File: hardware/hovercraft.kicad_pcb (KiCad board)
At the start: 2 copper layers, 50 x 65 mm, 44 parts, among them J1 USB_OTG, J10 CONN_01X02, J11 CONN_01X02, J12 CONN_01X02, J2 CONN_01X03, J3 CONN_01X03, J4 CONN_01X03, J5 CONN_01X03, J6 CONN_01X03, J7 CONN_01X03, J8 CONN_01X02, J9 CONN_01X02, SW1 RESET, SW2 BOOT, U1 HC-12, U2 ATMEGA32U2-AU, Y1 Crystal_GND24

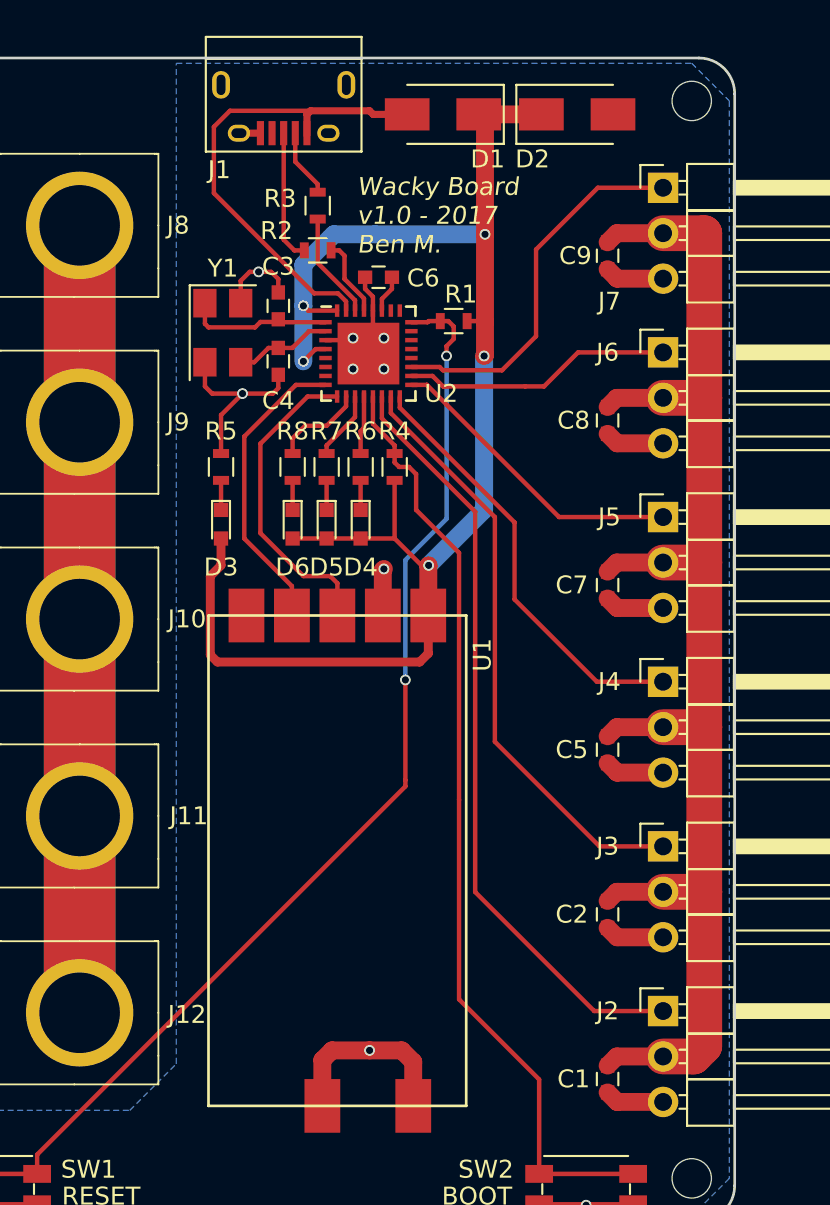
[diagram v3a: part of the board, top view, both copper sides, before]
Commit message: Moved the servo PWM signals to different pins to free up the SPI for a gyroscope/accelerometer/magnetometer
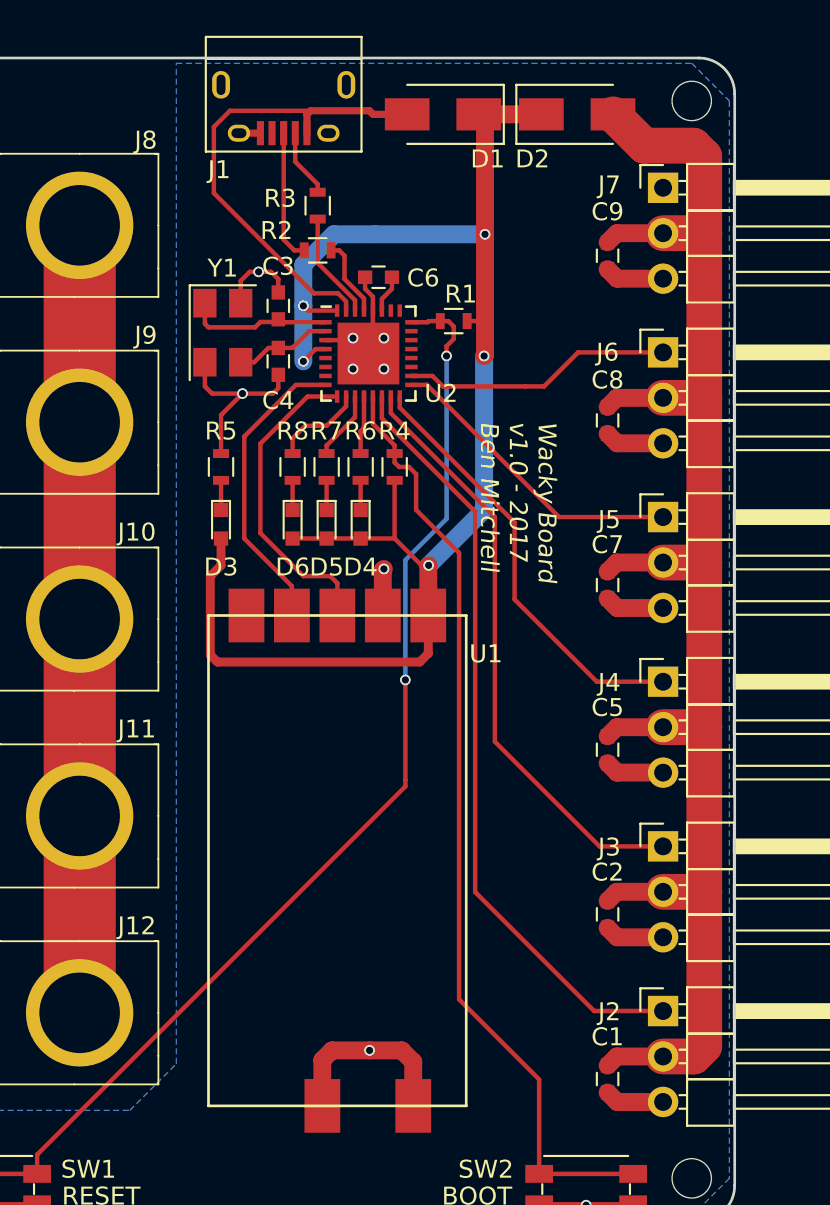
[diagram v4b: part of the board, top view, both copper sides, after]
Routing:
- net /CH5: track 21.2 -> 0.00 mm
- net Net-(C1-Pad1): track 79.3 -> 89.7 mm
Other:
- board text added: "Wacky Board v1.0 - 2017 Ben Mitchell"
- board text removed: "Wacky Board v1.0 - 2017 Ben M."
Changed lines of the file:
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@@
     (area 99.984999 100.004999 150.135001 165.155001)
     (thickness 1.6)
-    (drawings 11)
-    (tracks 288)
+    (drawings 13)
+    (tracks 285)
     (zones 0)
     (modules 44)
@@
   )
   (setup
-    (last_trace_width 0.25)
+    (last_trace_width 2)
     (user_trace_width 0.4)
     (user_trace_width 0.5)
@@
     (tags "capacitor 0603")
     (attr smd)
-    (fp_text reference C2 (at 0 2 360) (layer F.SilkS)
+    (fp_text reference C2 (at -2.35 0 360) (layer F.SilkS)
       (effects (font (size 1 1) (thickness 0.15)))
     )
@@
   (module modules:XT60 (layer F.Cu)
     (at 105.96 109.43)
-    (fp_text reference J8 (at 13 0) (layer F.SilkS)
+    (fp_text reference J8 (at 11.2 -4.75) (layer F.SilkS)
       (effects (font (size 1 1) (thickness 0.15)))
     )
@@
   (module modules:XT60 (layer F.Cu)
     (at 105.96 120.43)
-    (fp_text reference J9 (at 13 0) (layer F.SilkS)
+    (fp_text reference J9 (at 11.2 -4.85) (layer F.SilkS)
       (effects (font (size 1 1) (thickness 0.15)))
     )
@@
   (module modules:XT60 (layer F.Cu)
     (at 105.96 131.43)
-    (fp_text reference J10 (at 13.5 0) (layer F.SilkS)
+    (fp_text reference J10 (at 10.7 -4.85) (layer F.SilkS)
       (effects (font (size 1 1) (thickness 0.15)))
     )
@@
   (module modules:XT60 (layer F.Cu)
     (at 105.96 142.43)
-    (fp_text reference J11 (at 13.6 0) (layer F.SilkS)
+    (fp_text reference J11 (at 10.7 -4.85) (layer F.SilkS)
       (effects (font (size 1 1) (thickness 0.15)))
     )
@@
     (tags "capacitor 0603")
     (attr smd)
-    (fp_text reference C1 (at 0 1.9 360) (layer F.SilkS)
+    (fp_text reference C1 (at -2.35 0 360) (layer F.SilkS)
       (effects (font (size 1 1) (thickness 0.15)))
     )
@@
     (tags "capacitor 0603")
     (attr smd)
-    (fp_text reference C5 (at 0 2 360) (layer F.SilkS)
+    (fp_text reference C5 (at -2.35 0 360) (layer F.SilkS)
       (effects (font (size 1 1) (thickness 0.15)))
     )
@@
     (tags "capacitor 0603")
     (attr smd)
-    (fp_text reference C7 (at 0 2 360) (layer F.SilkS)
+    (fp_text reference C7 (at -2.25 0 360) (layer F.SilkS)
       (effects (font (size 1 1) (thickness 0.15)))
     )
@@
     (tags "capacitor 0603")
     (attr smd)
-    (fp_text reference C8 (at 0 1.9 360) (layer F.SilkS)
+    (fp_text reference C8 (at -2.25 0 360) (layer F.SilkS)
       (effects (font (size 1 1) (thickness 0.15)))
     )
@@
     (tags "capacitor 0603")
     (attr smd)
-    (fp_text reference C9 (at 0 1.8 360) (layer F.SilkS)
+    (fp_text reference C9 (at -2.45 0 360) (layer F.SilkS)
       (effects (font (size 1 1) (thickness 0.15)))
     )
@@
     (descr "Through hole angled pin header, 1x03, 2.54mm pitch, 6mm pin length, single row")
     (tags "Through hole angled pin header THT 1x03 2.54mm single row")
-    (fp_text reference J2 (at -3.1 0) (layer F.SilkS)
+    (fp_text reference J2 (at -3 0.05) (layer F.SilkS)
       (effects (font (size 1 1) (thickness 0.15)))
     )
@@
     (descr "Through hole angled pin header, 1x03, 2.54mm pitch, 6mm pin length, single row")
     (tags "Through hole angled pin header THT 1x03 2.54mm single row")
-    (fp_text reference J4 (at -3 0) (layer F.SilkS)
+    (fp_text reference J4 (at -3 0.05) (layer F.SilkS)
       (effects (font (size 1 1) (thickness 0.15)))
     )
@@
     (descr "Through hole angled pin header, 1x03, 2.54mm pitch, 6mm pin length, single row")
     (tags "Through hole angled pin header THT 1x03 2.54mm single row")
-    (fp_text reference J5 (at -3 0) (layer F.SilkS)
+    (fp_text reference J5 (at -3 0.15) (layer F.SilkS)
       (effects (font (size 1 1) (thickness 0.15)))
     )
@@
   (module modules:XT60 (layer F.Cu)
     (at 105.96 153.43)
-    (fp_text reference J12 (at 13.5 0.1) (layer F.SilkS)
+    (fp_text reference J12 (at 10.7 -4.85) (layer F.SilkS)
       (effects (font (size 1 1) (thickness 0.15)))
     )
@@
     (descr "Through hole angled pin header, 1x03, 2.54mm pitch, 6mm pin length, single row")
     (tags "Through hole angled pin header THT 1x03 2.54mm single row")
-    (fp_text reference J3 (at -3.1 0) (layer F.SilkS)
+    (fp_text reference J3 (at -3 0.05) (layer F.SilkS)
       (effects (font (size 1 1) (thickness 0.15)))
     )
@@
     (descr "Through hole angled pin header, 1x03, 2.54mm pitch, 6mm pin length, single row")
     (tags "Through hole angled pin header THT 1x03 2.54mm single row")
-    (fp_text reference J7 (at -3 6.35) (layer F.SilkS)
+    (fp_text reference J7 (at -3 -0.15) (layer F.SilkS)
       (effects (font (size 1 1) (thickness 0.15)))
     )
@@
   (module modules:HC-12 (layer F.Cu)
     (at 135.06 131.23 270)
-    (fp_text reference U1 (at 2.2 -0.9 270) (layer F.SilkS)
+    (fp_text reference U1 (at 2.15 -1.1 360) (layer F.SilkS)
       (effects (font (size 1 1) (thickness 0.15)))
     )
@@
     (fp_circle (center 0 0) (end 2.45 0) (layer F.CrtYd) (width 0.05))
     (pad 1 np_thru_hole circle (at 0 0) (size 2.2 2.2) (drill 2.2) (layers *.Cu *.Mask))
+  )
+  (dimension 65 (width 0.3) (layer Cmts.User)
+    (gr_text "65.000 mm" (at 162.31 132.58 270) (layer Cmts.User)
+      (effects (font (size 1.5 1.5) (thickness 0.3)))
+    )
+    (feature1 (pts (xy 147.66 165.08) (xy 163.66 165.08)))
+    (feature2 (pts (xy 147.66 100.08) (xy 163.66 100.08)))
+    (crossbar (pts (xy 160.96 100.08) (xy 160.96 165.08)))
+    (arrow1a (pts (xy 160.96 165.08) (xy 160.373579 163.953496)))
+    (arrow1b (pts (xy 160.96 165.08) (xy 161.546421 163.953496)))
+    (arrow2a (pts (xy 160.96 100.08) (xy 160.373579 101.206504)))
+    (arrow2b (pts (xy 160.96 100.08) (xy 161.546421 101.206504)))
+  )
+  (dimension 50 (width 0.3) (layer Cmts.User)
+    (gr_text "50.000 mm" (at 125.06 90.03) (layer Cmts.User)
+      (effects (font (size 1.5 1.5) (thickness 0.3)))
+    )
+    (feature1 (pts (xy 150.06 104.88) (xy 150.06 88.68)))
+    (feature2 (pts (xy 100.06 104.88) (xy 100.06 88.68)))
+    (crossbar (pts (xy 100.06 91.38) (xy 150.06 91.38)))
+    (arrow1a (pts (xy 150.06 91.38) (xy 148.933496 91.966421)))
+    (arrow1b (pts (xy 150.06 91.38) (xy 148.933496 90.793579)))
+    (arrow2a (pts (xy 100.06 91.38) (xy 101.186504 91.966421)))
+    (arrow2b (pts (xy 100.06 91.38) (xy 101.186504 90.793579)))
   )
   (gr_line (start 100.06 163.08) (end 100.06 102.08) (layer Edge.Cuts) (width 0.15))
@@
   (gr_arc (start 102.06 163.08) (end 102.06 165.08) (angle 90) (layer Edge.Cuts) (width 0.15))
   (gr_arc (start 102.06 102.08) (end 100.06 102.08) (angle 90) (layer Edge.Cuts) (width 0.15))
-  (gr_text "Wacky Board\nv1.0 - 2017\nBen M." (at 128.96 108.88) (layer F.SilkS)
+  (gr_text "Wacky Board\nv1.0 - 2017\nBen Mitchell" (at 137.96 120.38 270) (layer F.SilkS)
     (effects (font (size 1 1) (thickness 0.15) italic) (justify left))
   )
@@
   (segment (start 136.66 138.28) (end 136.66 125.73) (width 0.25) (layer F.Cu) (net 13))
   (segment (start 137.76 130.33) (end 142.36 134.93) (width 0.25) (layer F.Cu) (net 14))
+  (segment (start 137.76 130.33) (end 137.76 126.03) (width 0.25) (layer F.Cu) (net 14))
+  (segment (start 137.76 126.03) (end 131.3473 119.6173) (width 0.25) (layer F.Cu) (net 14))
+  (segment (start 131.3473 119.6173) (end 131.3473 118.9951) (width 0.25) (layer F.Cu) (net 14))
   (segment (start 142.36 134.93) (end 146.06 134.93) (width 0.25) (layer F.Cu) (net 14))
-  (segment (start 131.3473 119.6173) (end 131.3473 118.9951) (width 0.25) (layer F.Cu) (net 14))
-  (segment (start 137.76 126.03) (end 131.3473 119.6173) (width 0.25) (layer F.Cu) (net 14))
-  (segment (start 137.76 130.33) (end 137.76 126.03) (width 0.25) (layer F.Cu) (net 14))
   (segment (start 132.86 118.3451) (end 140.2449 125.73) (width 0.25) (layer F.Cu) (net 15))
   (segment (start 140.2449 125.73) (end 146.06 125.73) (width 0.25) (layer F.Cu) (net 15))
@@
   (segment (start 134.36 115.78) (end 134.36 115.08) (width 0.25) (layer F.Cu) (net 20))
   (segment (start 133.96 116.18) (end 134.36 115.78) (width 0.25) (layer F.Cu) (net 20))
+  (segment (start 148.36 109.87) (end 148.36 105.58) (width 2) (layer F.Cu) (net 21))
+  (segment (start 145.01 104.98) (end 143.26 103.23) (width 2) (layer F.Cu) (net 21))
+  (segment (start 147.76 104.98) (end 145.01 104.98) (width 2) (layer F.Cu) (net 21))
+  (segment (start 148.36 105.58) (end 147.76 104.98) (width 2) (layer F.Cu) (net 21))
   (segment (start 146.06 109.87) (end 148.36 109.87) (width 2) (layer F.Cu) (net 21))
   (segment (start 146.06 119.07) (end 148.36 119.07) (width 2) (layer F.Cu) (net 21))
@@
   (segment (start 129.16 125.33) (end 129.16 123.68) (width 0.25) (layer F.Cu) (net 24))
   (segment (start 127.26 123.68) (end 127.26 125.33) (width 0.25) (layer F.Cu) (net 25))
-  (segment (start 137.06 117.53) (end 138.96 115.63) (width 0.25) (layer F.Cu) (net 27))
-  (segment (start 138.96 115.63) (end 138.96 110.78) (width 0.25) (layer F.Cu) (net 27))
-  (segment (start 138.96 110.78) (end 142.41 107.33) (width 0.25) (layer F.Cu) (net 27))
-  (segment (start 142.41 107.33) (end 146.06 107.33) (width 0.25) (layer F.Cu) (net 27))
-  (segment (start 133.5751 117.3451) (end 131.9973 117.3451) (width 0.25) (layer F.Cu) (net 27))
-  (segment (start 133.76 117.53) (end 133.5751 117.3451) (width 0.25) (layer F.Cu) (net 27))
-  (segment (start 137.06 117.53) (end 133.76 117.53) (width 0.25) (layer F.Cu) (net 27))
   (segment (start 134.66 152.68) (end 139.135 157.155) (width 0.25) (layer F.Cu) (net 28))
   (segment (start 144.385 162.43) (end 139.135 162.43) (width 0.25) (layer F.Cu) (net 28))
